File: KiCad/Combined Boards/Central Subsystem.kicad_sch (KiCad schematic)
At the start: 0 parts

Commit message: Started Central Subsystem
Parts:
- added C1, C2: 3.3 pF, symbol Device:C_Small
- added C10, C5: 1.8 pF, symbol Device:C_Small
- added C11: 47 pF, symbol Device:C_Small
- added C12: 2.4 pF, symbol Device:C_Small
- added C13: 47 nF, symbol Device:C_Small
- added C3, C7: 39 pF, symbol Device:C_Small
- added C4: 100 nF, symbol Device:C_Small
- added C6: 1 nF, symbol Device:C_Small
- added C8: 5.6 pF, symbol Device:C_Small
- added C9: 3.0 pF, symbol Device:C_Small
- added J1: Antenna, digikey-footprints:Coax_Conn_U.FL, symbol dk_Coaxial-Connectors-RF:U_FL-R-SMT_10_
- added L1: 9.1 nH, symbol Device:L_Small
- added L2: 4.7 nH, symbol Device:L_Small
- added L3: 2.5 nH, symbol Device:L_Small
- added L4: 47 nH, symbol Device:L_Small
- added L5: 15 nH, symbol Device:L_Small
- added R2: 100, symbol Device:R_Small_US
- added U1: STM32WLE5CCU6, Package_DFN_QFN:QFN-48-1EP_7x7mm_P0.5mm_EP5.6x5.6mm, symbol MCU_ST_STM32WL:STM32WLE5CCUx
- added U4: ~, symbol Wireless Sensors:HMC8038
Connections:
- new net: C5.1, L2.1, U4.9 (RF1)
- new net: C7.1, L2.2
- new net: C11.1, C13.1, L4.2, U1.24 (VR_PA)
- new net: C12.1, U4.12 (RF2)
- new net: C6.1, R2.1, U4.2 (VCTL)
- new net: C3.2, U4.3 (RFC)
- new net: C1.1, J1.2, L1.1
- new net: C12.2, L5.1, U1.21 (RFI_N)
- new net: C10.1, L5.2, U1.20 (RFI_P)
- new net: C2.1, C3.1, L1.2
- new net: C7.2, C8.1, C9.1, L3.1
- new net: C9.2, L3.2, L4.1, U1.23 (RFO_HP)
- new net: R2.2, U1.38 (PC13)
- new net +3.3V: C4.1, U4.1 (VDD)
- new net GND: C1.2, C10.2, C11.2, C13.2, C2.2, C4.2, C5.2, C6.2, C8.2, J1.1, U4.10 (GND), U4.11 (GND), U4.5 (EN)
- no-connect marks 0 -> 8

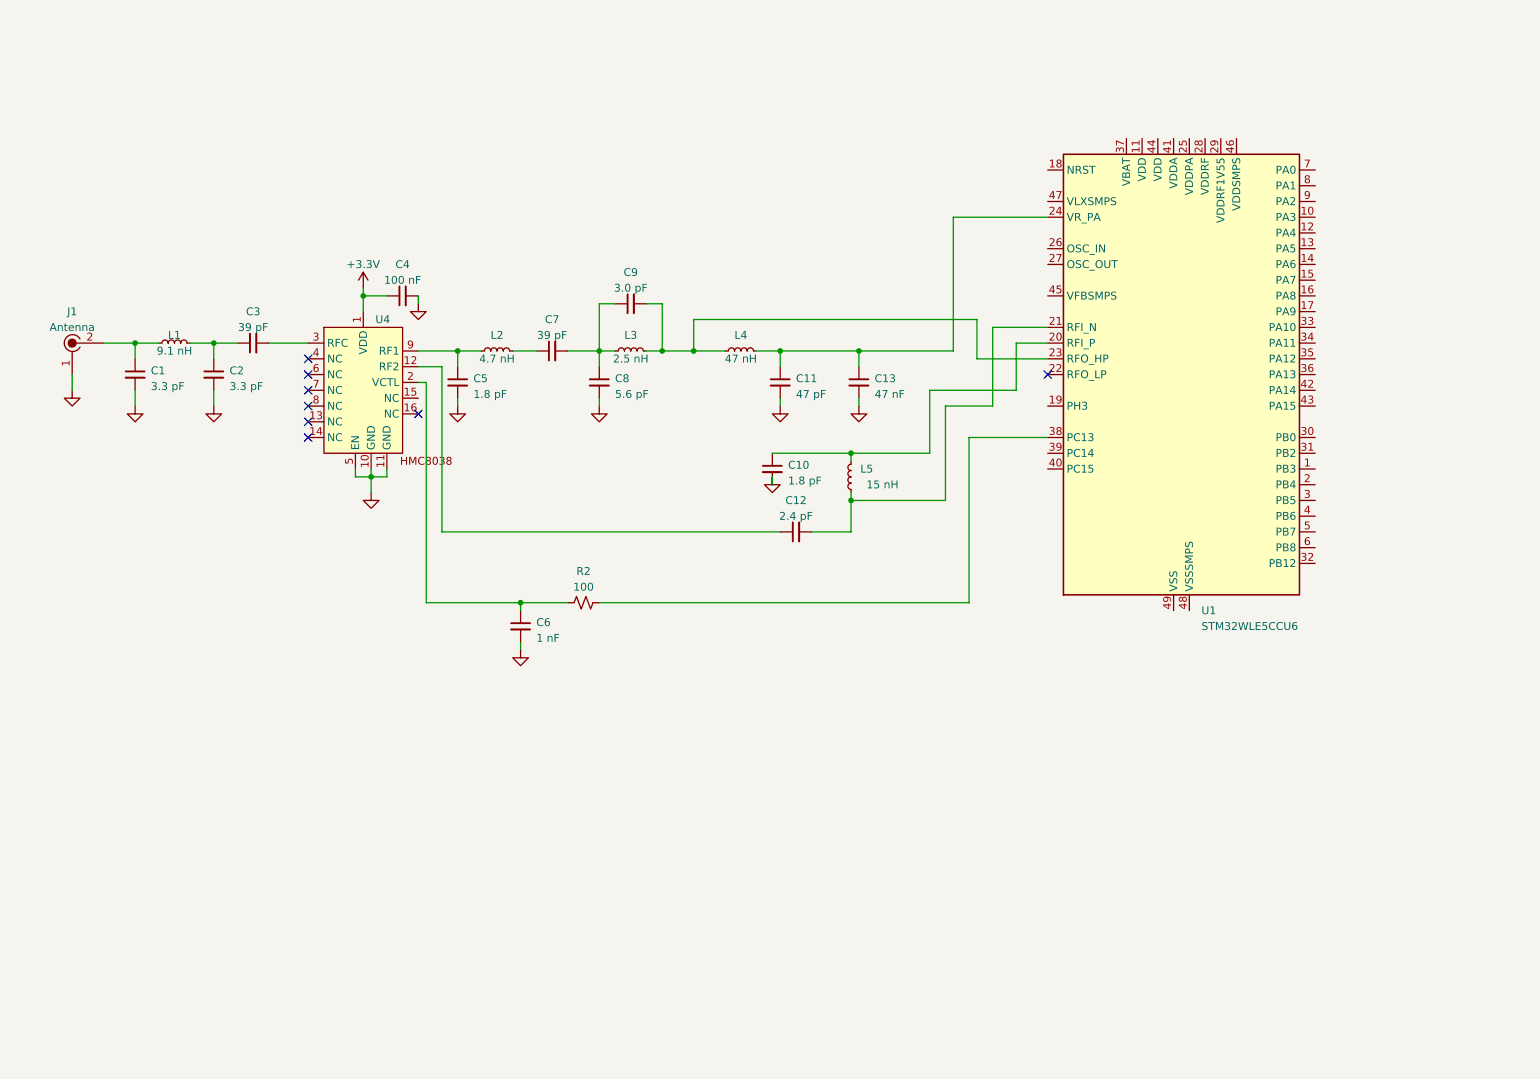
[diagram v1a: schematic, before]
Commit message: Central subsystem design
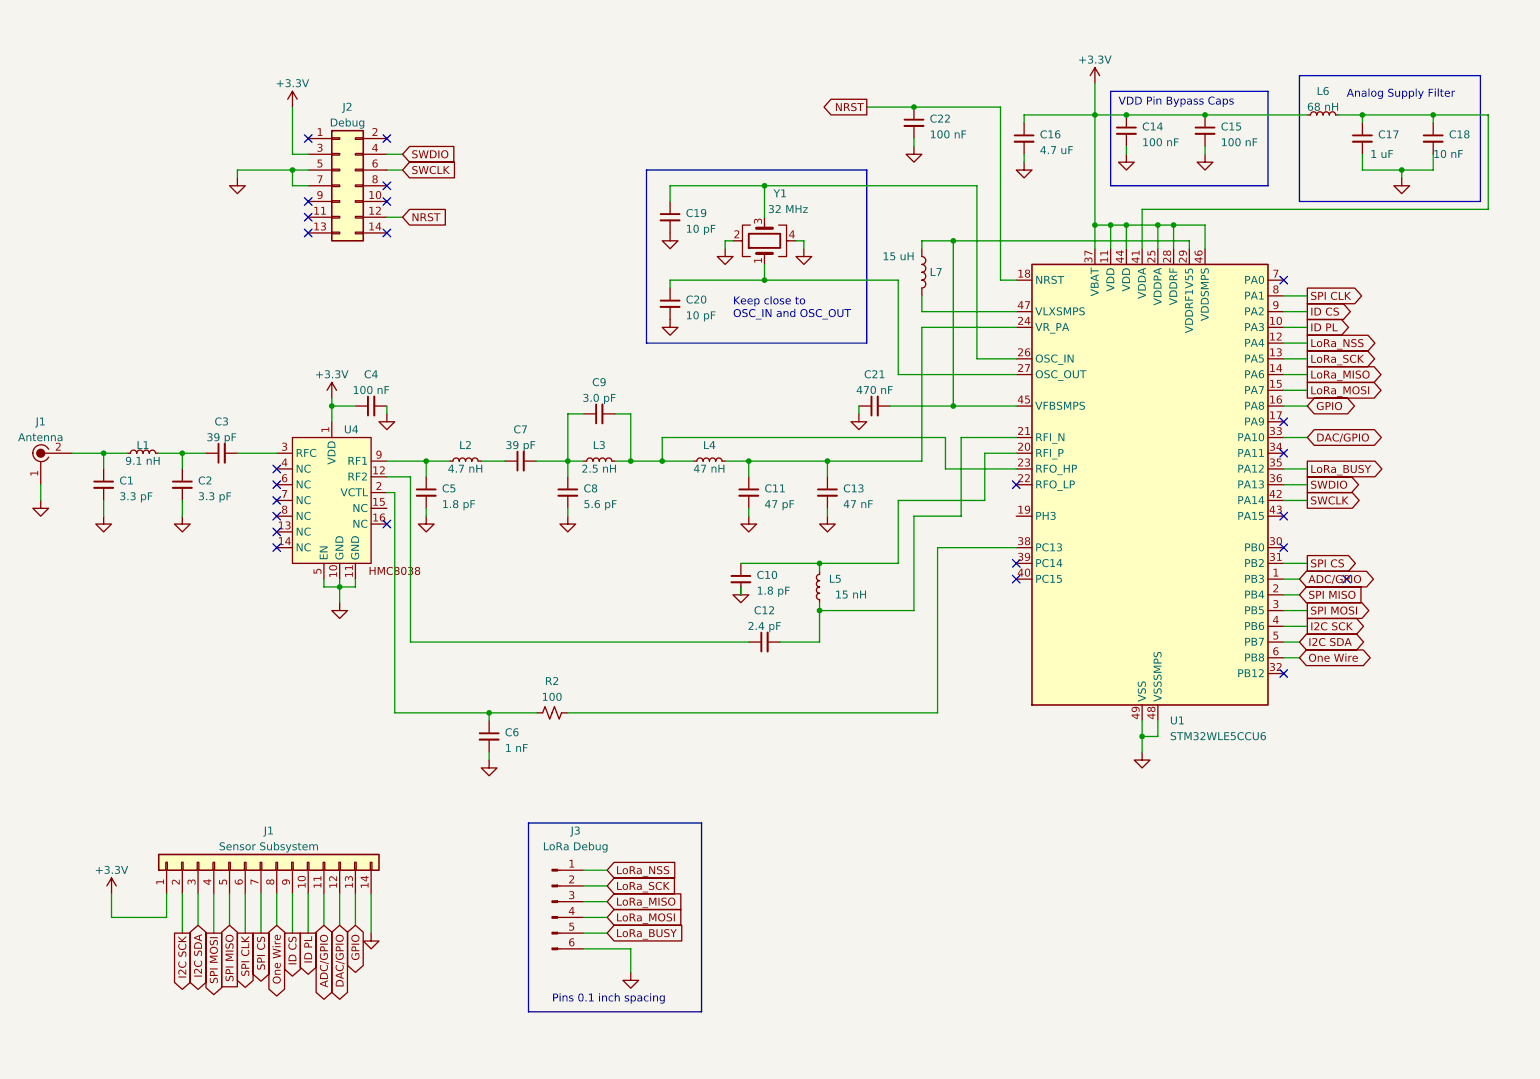
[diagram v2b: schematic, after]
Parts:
- added C14, C15, C22: 100 nF, symbol Device:C_Small
- added C16: 4.7 uF, symbol Device:C_Small
- added C17: 1 uF, symbol Device:C_Small
- added C18: 10 nF, symbol Device:C_Small
- added C19, C20: 10 pF, symbol Device:C_Small
- added C21: 470 nF, symbol Device:C_Small
- added J1: Sensor Subsystem, symbol Connector_Generic:Conn_01x14
- added J2: Debug, symbol Connector_Generic:Conn_02x07_Odd_Even
- added J3: LoRa Debug, symbol Connector:Conn_01x06_Pin
- added L6: 68 nH, symbol Device:L_Small
- added L7: 15 uH, symbol Device:L
- added Y1: 32 MHz, symbol Device:Crystal_GND24
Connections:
- net +3.3V: now also U1.11 (VDD), U1.25 (VDDPA), U1.28 (VDDRF), U1.37 (VBAT), U1.44 (VDD), U1.46 (VDDSMPS), C14.1, C15.1, C16.1, J1.1 (Pin_1), J2.3 (Pin_3), L6.1
- net GND: now also U1.48 (VSSSMPS), U1.49 (VSS), C14.2, C15.2, C16.2, C17.2, C18.2, C19.2, C20.2, C21.1, C22.2, J1.14 (Pin_14), J2.5 (Pin_5), J2.7 (Pin_7), J3.6 (Pin_6), Y1.2, Y1.4
- net ADC/GPIO: now reaches U1.1 (PB3)
- net ADC/GPIO: now also J1.11 (Pin_11)
- net ID PL: now reaches U1.10 (PA3)
- net ID PL: now also J1.10 (Pin_10)
- net LoRa_NSS: now reaches U1.12 (PA4)
- net LoRa_NSS: now also J3.1 (Pin_1)
- net LoRa_SCK: now reaches U1.13 (PA5)
- net LoRa_SCK: now also J3.2 (Pin_2)
- net LoRa_MISO: now reaches U1.14 (PA6)
- net LoRa_MISO: now also J3.3 (Pin_3)
- net LoRa_MOSI: now reaches U1.15 (PA7)
- net LoRa_MOSI: now also J3.4 (Pin_4)
- net GPIO: now reaches U1.16 (PA8)
- net GPIO: now also J1.13 (Pin_13)
- net NRST: now reaches U1.18 (NRST)
- net NRST: now also C22.1, J2.12 (Pin_12)
- net SPI MISO: now reaches U1.2 (PB4)
- net SPI MISO: now also J1.5 (Pin_5)
- net at U1.26 (OSC_IN): now also C19.1, Y1.3
- net at U1.27 (OSC_OUT): now also C20.1, Y1.1
- net at U1.29 (VDDRF1V55): now also U1.45 (VFBSMPS), C21.2, L7.1
- net SPI MOSI: now reaches U1.3 (PB5)
- net SPI MOSI: now also J1.4 (Pin_4)
- net SPI CS: now reaches U1.31 (PB2)
- net SPI CS: now also J1.7 (Pin_7)
- net DAC/GPIO: now reaches U1.33 (PA10)
- net DAC/GPIO: now also J1.12 (Pin_12)
- net LoRa_BUSY: now reaches U1.35 (PA12)
- net LoRa_BUSY: now also J3.5 (Pin_5)
- net SWDIO: now reaches U1.36 (PA13)
- net SWDIO: now also J2.4 (Pin_4)
- net I2C SCK: now reaches U1.4 (PB6)
- net I2C SCK: now also J1.2 (Pin_2)
- net at U1.41 (VDDA): now also C17.1, C18.1, L6.2
- net SWCLK: now reaches U1.42 (PA14)
- net SWCLK: now also J2.6 (Pin_6)
- net at U1.47 (VLXSMPS): now also L7.2
- net I2C SDA: now reaches U1.5 (PB7)
- net I2C SDA: now also J1.3 (Pin_3)
- net One Wire: now reaches U1.6 (PB8)
- net One Wire: now also J1.8 (Pin_8)
- net SPI CLK: now reaches U1.8 (PA1)
- net SPI CLK: now also J1.6 (Pin_6)
- net ID CS: now reaches U1.9 (PA2)
- net ID CS: now also J1.9 (Pin_9)
- no-connect marks 8 -> 25
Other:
- note added: "Analog Supply Filter"
- note added: "Keep close to OSC_IN and OSC_OUT"
- note added: "Pins 0.1 inch spacing"
- note added: "VDD Pin Bypass Caps"
- moved on the sheet: C1, C10, C11, C12, C13, C2, C3, C4, C5, C6, C7, C8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

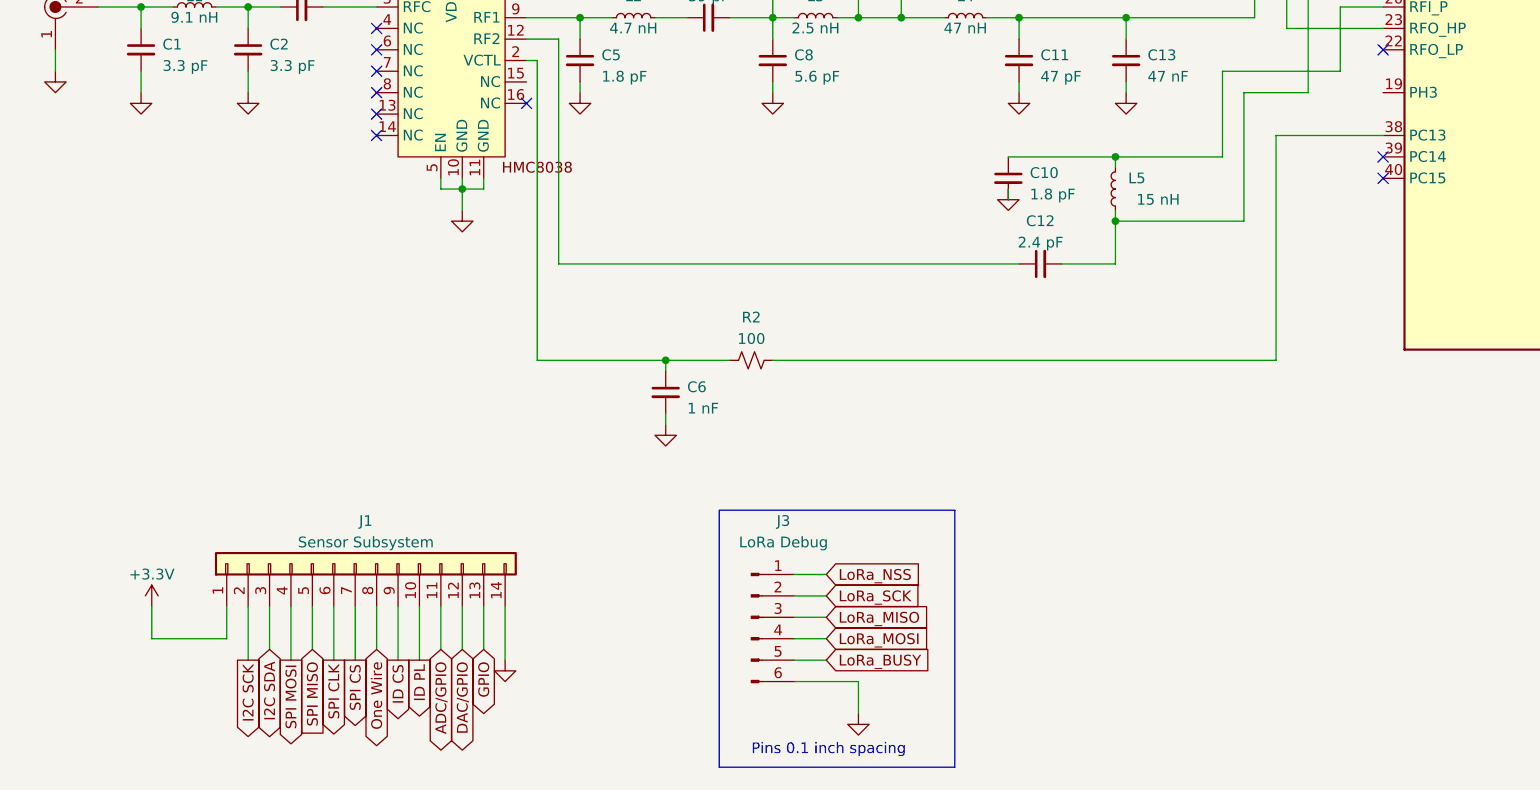
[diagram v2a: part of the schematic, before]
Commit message: Added FET to switch sensor power
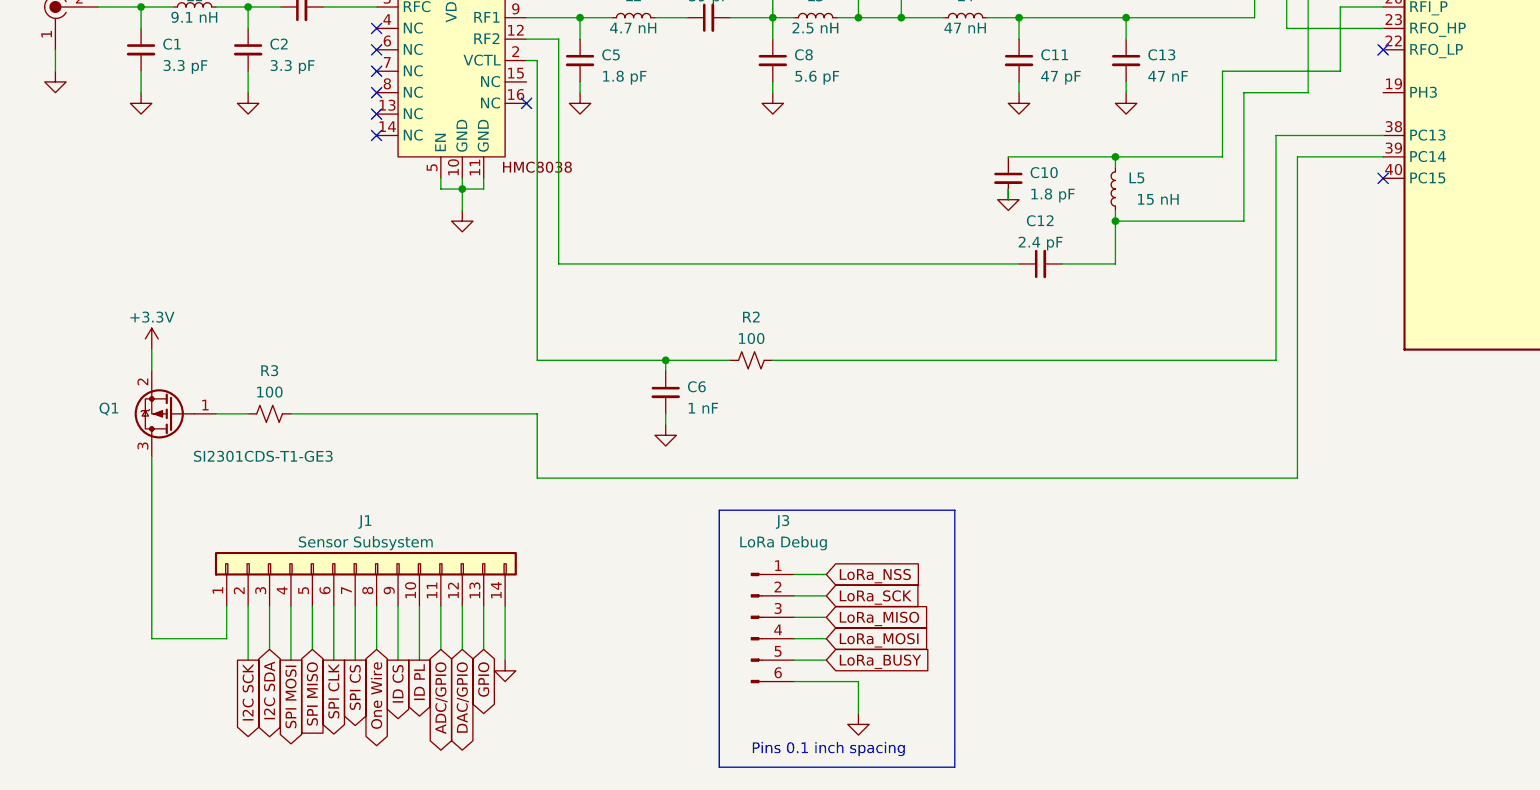
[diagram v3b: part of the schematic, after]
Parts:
- added Q1: SI2301CDS-T1-GE3, Package_TO_SOT_SMD:SOT-23, symbol Transistor_FET:Si2319CDS
- added R3: 100, symbol Device:R_Small_US
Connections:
- net +3.3V: now also Q1.2 (S); no longer J1.1 (Pin_1)
- net at U1.39 (PC14): now also R3.2
- new net: Q1.1 (G), R3.1
- new net: J1.1 (Pin_1), Q1.3 (D)
- no-connect marks 25 -> 24
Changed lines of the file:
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@@
   (no_connect (at 62.23 53.34))
   (no_connect (at 219.71 60.96))
-  (no_connect (at 176.53 106.68))
   (no_connect (at 219.71 88.9))
   (no_connect (at 57.15 93.98))
@@
     (stroke (width 0) (type default))
   )
+  (wire (pts (xy 30.48 129.54) (xy 30.48 132.08))
+    (stroke (width 0) (type default))
+  )
   (wire (pts (xy 238.76 43.18) (xy 238.76 44.45))
     (stroke (width 0) (type default))
@@
     (stroke (width 0) (type default))
   )
-  (wire (pts (xy 30.48 160.02) (xy 30.48 163.83))
+  (wire (pts (xy 166.37 106.68) (xy 166.37 144.78))
     (stroke (width 0) (type default))
   )
@@
     (stroke (width 0) (type default))
   )
+  (wire (pts (xy 30.48 142.24) (xy 30.48 163.83))
+    (stroke (width 0) (type default))
+  )
   (wire (pts (xy 189.23 52.07) (xy 189.23 55.88))
     (stroke (width 0) (type default))
@@
     (stroke (width 0) (type default))
   )
+  (wire (pts (xy 76.2 144.78) (xy 76.2 137.16))
+    (stroke (width 0) (type default))
+  )
   (wire (pts (xy 207.01 39.37) (xy 207.01 40.64))
     (stroke (width 0) (type default))
@@
     (stroke (width 0) (type default))
   )
+  (wire (pts (xy 166.37 144.78) (xy 76.2 144.78))
+    (stroke (width 0) (type default))
+  )
   (wire (pts (xy 165.1 91.44) (xy 165.1 86.36))
     (stroke (width 0) (type default))
@@
     (stroke (width 0) (type default))
   )
+  (wire (pts (xy 38.1 137.16) (xy 41.91 137.16))
+    (stroke (width 0) (type default))
+  )
   (wire (pts (xy 74.93 43.18) (xy 77.47 43.18))
     (stroke (width 0) (type default))
@@
     (stroke (width 0) (type default))
   )
+  (wire (pts (xy 76.2 137.16) (xy 46.99 137.16))
+    (stroke (width 0) (type default))
+  )
   (wire (pts (xy 106.68 90.17) (xy 104.14 90.17))
     (stroke (width 0) (type default))
@@
   )
   (wire (pts (xy 161.29 55.88) (xy 161.29 54.61))
+    (stroke (width 0) (type default))
+  )
+  (wire (pts (xy 176.53 106.68) (xy 166.37 106.68))
     (stroke (width 0) (type default))
   )
@@
         (path "/81d1aadf-85d2-4fd0-839e-05ac66879581"
           (reference "L4") (unit 1)
+        )
+      )
+    )
+  )
+  (symbol (lib_id "Transistor_FET:Si2319CDS") (at 33.02 137.16 180) (unit 1)
+    (in_bom yes) (on_board yes) (dnp no)
+    (property "Reference" "Q1" (at 26.67 136.525 0)
+      (effects (font (size 1.27 1.27)) (justify left))
+    )
+    (property "Value" "SI2301CDS-T1-GE3" (at 52.07 142.24 0)
+      (effects (font (size 1.27 1.27)) (justify left))
+    )
+    (property "Footprint" "Package_TO_SOT_SMD:SOT-23" (at 27.94 135.255 0)
+      (effects (font (size 1.27 1.27) italic) (justify left) hide)
+    )
+    (property "Datasheet" "http://www.vishay.com/docs/66709/si2319cd.pdf" (at 33.02 137.16 0)
+      (effects (font (size 1.27 1.27)) (justify left) hide)
+    )
+    (pin "1")
+    (pin "2")
+    (pin "3")
+    (instances
+      (project "Combined Boards"
+        (path "/819f9f2e-5083-42df-b63a-6cdcb84600f5/1dc5bc9e-b621-49d0-a745-1efaf62549e2"
+          (reference "Q1") (unit 1)
         )
       )
@@
     )
   )
+  (symbol (lib_id "Device:R_Small_US") (at 44.45 137.16 90) (unit 1)
+    (in_bom yes) (on_board yes) (dnp no) (fields_autoplaced)
+    (property "Reference" "R3" (at 44.45 132.08 90)
+      (effects (font (size 1.27 1.27)))
+    )
+    (property "Value" "100" (at 44.45 134.62 90)
+      (effects (font (size 1.27 1.27)))
+    )
+    (property "Footprint" "" (at 44.45 137.16 0)
+      (effects (font (size 1.27 1.27)) hide)
+    )
+    (property "Datasheet" "~" (at 44.45 137.16 0)
+      (effects (font (size 1.27 1.27)) hide)
+    )
+    (pin "1")
+    (pin "2")
+    (instances
+      (project "Combined Boards"
+        (path "/819f9f2e-5083-42df-b63a-6cdcb84600f5/1dc5bc9e-b621-49d0-a745-1efaf62549e2"
+          (reference "R3") (unit 1)
+        )
+      )
+      (project "LoRa Development Board"
+        (path "/81d1aadf-85d2-4fd0-839e-05ac66879581"
+          (reference "R1") (unit 1)
+        )
+      )
+    )
+  )
   (symbol (lib_id "power:GND") (at 74.93 82.55 0) (unit 1)
     (in_bom yes) (on_board yes) (dnp no) (fields_autoplaced)
@@
     )
   )
-  (symbol (lib_id "power:+3.3V") (at 30.48 160.02 0) (unit 1)
-    (in_bom yes) (on_board yes) (dnp no) (fields_autoplaced)
-    (property "Reference" "#PWR01" (at 30.48 163.83 0)
-      (effects (font (size 1.27 1.27)) hide)
-    )
-    (property "Value" "+3.3V" (at 30.48 156.21 0)
-      (effects (font (size 1.27 1.27)))
-    )
-    (property "Footprint" "" (at 30.48 160.02 0)
-      (effects (font (size 1.27 1.27)) hide)
-    )
-    (property "Datasheet" "" (at 30.48 160.02 0)
-      (effects (font (size 1.27 1.27)) hide)
-    )
+  (symbol (lib_id "power:+3.3V") (at 30.48 129.54 0) (unit 1)
+    (in_bom yes) (on_board yes) (dnp no) (fields_autoplaced)
+    (property "Reference" "#PWR01" (at 30.48 133.35 0)
+      (effects (font (size 1.27 1.27)) hide)
+    )
+    (property "Value" "+3.3V" (at 30.48 125.73 0)
+      (effects (font (size 1.27 1.27)))
+    )
+    (property "Footprint" "" (at 30.48 129.54 0)
+      (effects (font (size 1.27 1.27)) hide)
+    )
+    (property "Datasheet" "" (at 30.48 129.54 0)
+      (effects (font (size 1.27 1.27)) hide)
+    )
